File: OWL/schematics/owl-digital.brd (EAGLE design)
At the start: 59.6 x 55.9 mm, 69 parts, among them IC1 REG1117, IC3 IS61WV51216BLL-10TLI, Q1 12.288MHz, Q2 8MHz, U2 WM8731, U4 STM32F405ZGT6

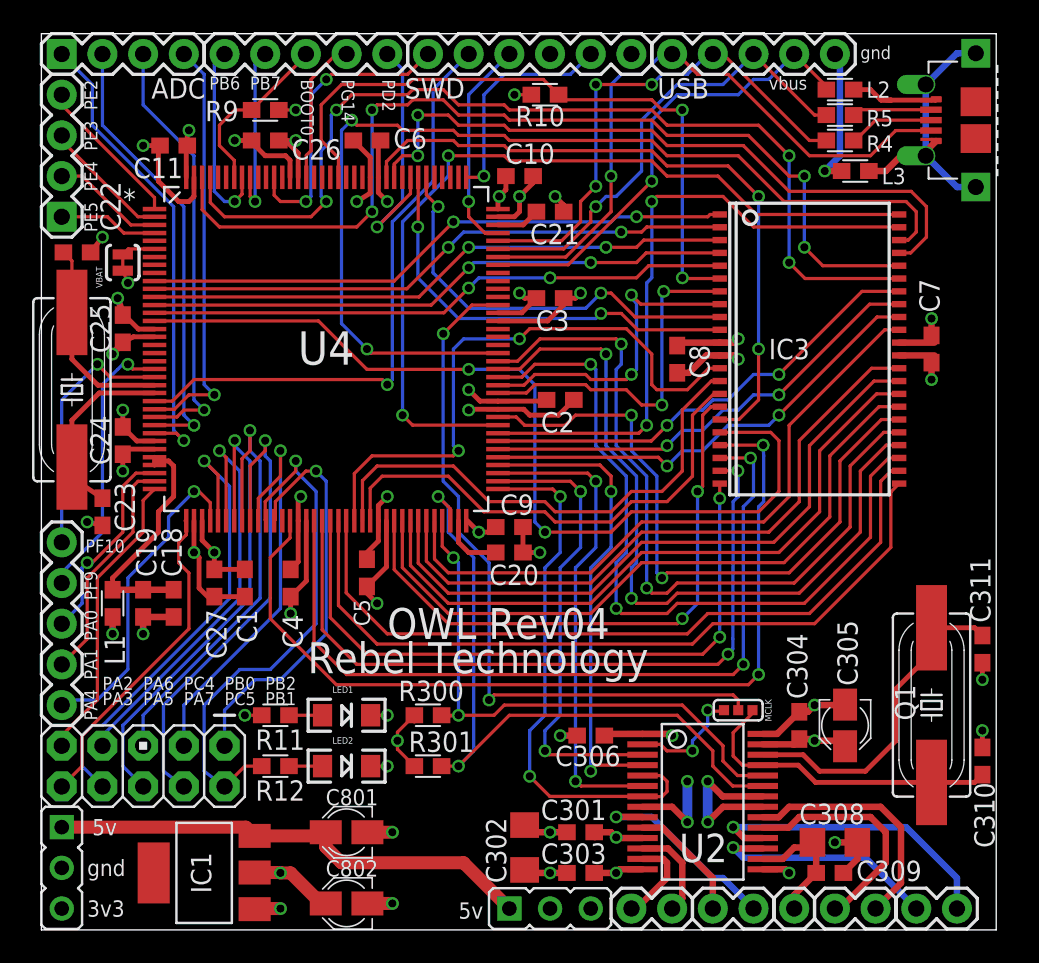
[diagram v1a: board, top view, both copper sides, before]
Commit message: changed for rev05: usb power routing via inductors, connected usb gnd.
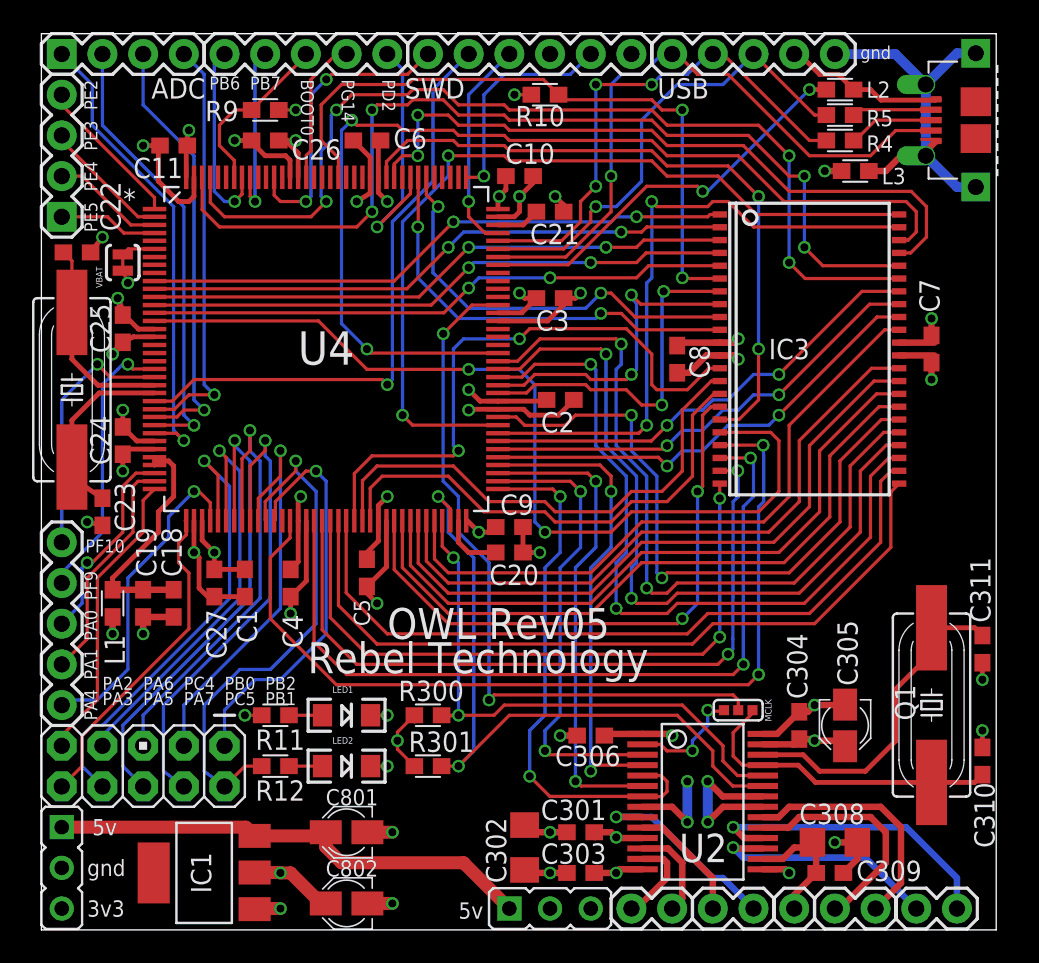
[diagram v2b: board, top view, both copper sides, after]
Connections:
- removed net N$1: L2.1, USB1.1, USB1.6
- removed net N$3: L3.1, USB1.5, USB1.7, USB1.G, USB1.G2, USB1.G3, USB1.G4
- new net VBUS: L2.2, U4.101
- net GND: now also L3.2
- net USB_GND: now also L3.1, USB1.5, USB1.7, USB1.G, USB1.G2, USB1.G3, USB1.G4; no longer L3.2
- net USB_VBUS: now also L2.1, USB1.1, USB1.6; no longer L2.2, U4.101
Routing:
- net VBUS: track 0.00 -> 25.3 mm, vias 0 -> 2
- net USB_VBUS: track 29.2 -> 11.0 mm, vias 1 -> 0
- net N$3: track 17.5 -> 0.00 mm
- net USB_GND: track 8.88 -> 23.9 mm, vias 1 -> 0
- net N$1: track 6.67 -> 0.00 mm
- net GND: track 111.6 -> 113.1 mm, vias 34 -> 35
- net +3V3: track 93.8 -> 94.8 mm
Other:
- board text added: "OWL Rev05"
- board text removed: "OWL Rev04"
- board text removed: "vbus"

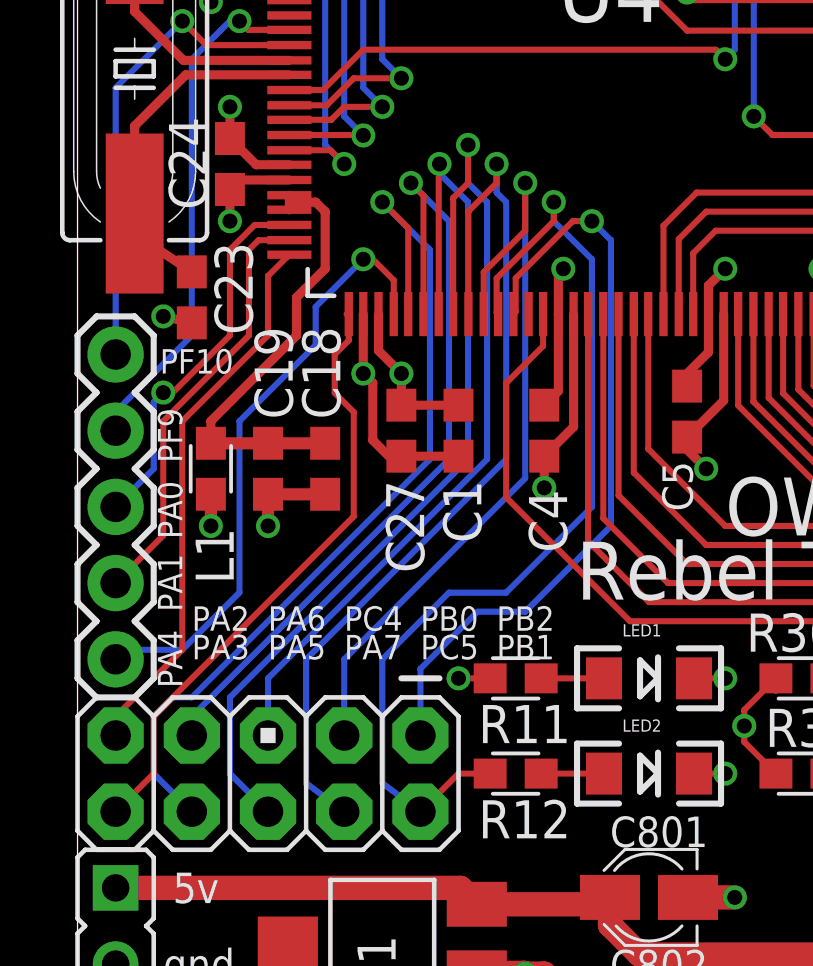
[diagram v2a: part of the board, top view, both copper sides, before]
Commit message: added pull-down resistor R13 from BOOT1/PD2 to gnd and tidied up schematic
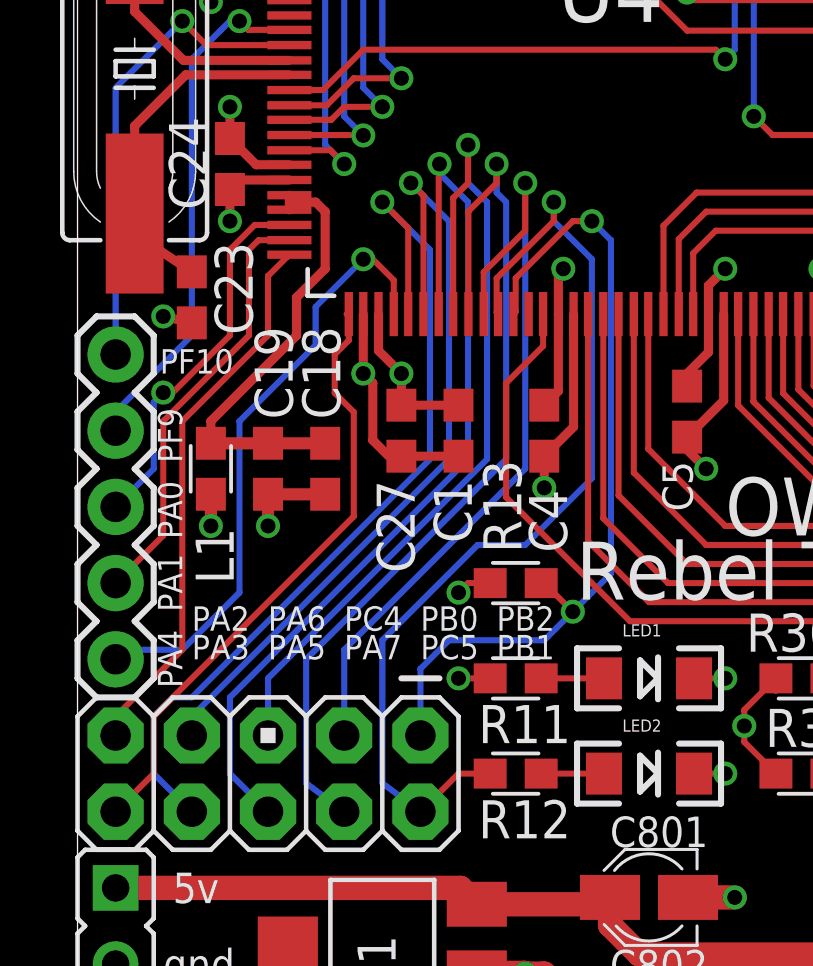
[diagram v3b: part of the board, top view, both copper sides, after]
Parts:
- added R13: 10K, Rebel:0603
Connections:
- removed net N$123: U4.19
- removed net N$124: U4.18
- net GND: now also R13.1
- net PB2: now also R13.2
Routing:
- net PB2: track 25.5 -> 27.9 mm, vias 1 -> 2
- net GND: track 113.1 -> 114.3 mm, vias 35 -> 36
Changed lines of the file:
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@@
 </element>
 <element name="C1" library="resistor" package="C0603" value="1u" x="12.7" y="22.225" smashed="yes" rot="R270">
-<attribute name="NAME" x="12.192" y="20.574" size="1.27" layer="25" rot="R270"/>
+<attribute name="NAME" x="11.8745" y="20.574" size="1.27" layer="25" rot="R270"/>
 <attribute name="VALUE" x="10.668" y="23.114" size="1.27" layer="27" rot="R270"/>
 </element>
@@
 </element>
 <element name="C27" library="resistor" package="C0603" value="100n" x="10.795" y="22.225" smashed="yes" rot="R270">
-<attribute name="NAME" x="10.287" y="20.574" size="1.27" layer="25" rot="R270"/>
+<attribute name="NAME" x="9.9695" y="20.574" size="1.27" layer="25" rot="R270"/>
 <attribute name="VALUE" x="8.763" y="23.114" size="1.27" layer="27" rot="R270"/>
 </element>
@@
 <attribute name="NAME" x="45.16954375" y="13.58138125" size="0.4064" layer="25" rot="R90" align="top-left"/>
 <attribute name="VALUE" x="44.7675" y="15.5575" size="0.4064" layer="27" rot="R180"/>
+</element>
+<element name="R13" library="Rebel" package="0603" value="10K" x="14.605" y="17.145" smashed="yes">
+<attribute name="NAME" x="14.7955" y="18.161" size="1.27" layer="25" rot="R90"/>
 </element>
 </elements>
@@
 <wire x1="50.165" y1="14.635" x2="49.7475" y2="14.635" width="0.4064" layer="1"/>
 <wire x1="49.7475" y1="14.635" x2="49.7175" y2="14.605" width="0.4064" layer="1"/>
+<contactref element="R13" pad="1"/>
+<wire x1="13.755" y1="17.145" x2="13.0175" y2="17.145" width="0.2032" layer="1"/>
+<wire x1="13.0175" y1="17.145" x2="12.7" y2="16.8275" width="0.2032" layer="1"/>
+<via x="12.7" y="16.8275" extent="1-16" drill="0.5"/>
 </signal>
 <signal name="+5V">
@@
 <contactref element="U4" pad="46"/>
 <via x="14.9225" y="30.48" extent="1-16" drill="0.5"/>
-<wire x1="14.9225" y1="30.48" x2="14.9225" y2="20.6375" width="0.2032" layer="16"/>
-<wire x1="14.9225" y1="20.6375" x2="8.89" y2="14.605" width="0.2032" layer="16"/>
-<wire x1="8.89" y1="14.605" x2="8.89" y2="12.065" width="0.2032" layer="16"/>
+<wire x1="14.9225" y1="30.48" x2="14.9225" y2="20.955" width="0.2032" layer="16"/>
+<wire x1="14.9225" y1="20.955" x2="8.89" y2="14.9225" width="0.2032" layer="16"/>
+<wire x1="8.89" y1="14.9225" x2="8.89" y2="12.065" width="0.2032" layer="16"/>
 <wire x1="13.5382" y1="26.1112" x2="13.5382" y2="27.5082" width="0.2032" layer="1"/>
 <wire x1="13.5382" y1="27.5082" x2="14.9225" y2="28.8925" width="0.2032" layer="1"/>
@@
 <via x="15.875" y="29.845" extent="1-16" drill="0.5"/>
 <wire x1="15.875" y1="29.845" x2="15.875" y2="29.21" width="0.2032" layer="16"/>
-<wire x1="17.145" y1="27.94" x2="17.145" y2="19.685" width="0.2032" layer="16"/>
-<wire x1="17.145" y1="19.685" x2="14.2875" y2="16.8275" width="0.2032" layer="16"/>
-<wire x1="14.2875" y1="16.8275" x2="12.3825" y2="16.8275" width="0.2032" layer="16"/>
-<wire x1="12.3825" y1="16.8275" x2="10.16" y2="14.605" width="0.2032" layer="16"/>
-<wire x1="10.16" y1="14.605" x2="10.16" y2="10.4775" width="0.2032" layer="16"/>
+<wire x1="17.145" y1="27.94" x2="17.145" y2="20.6375" width="0.2032" layer="16"/>
+<wire x1="17.145" y1="20.6375" x2="14.9225" y2="18.415" width="0.2032" layer="16"/>
+<wire x1="14.9225" y1="18.415" x2="13.335" y2="18.415" width="0.2032" layer="16"/>
+<wire x1="13.335" y1="18.415" x2="10.16" y2="15.24" width="0.2032" layer="16"/>
+<wire x1="10.16" y1="15.24" x2="10.16" y2="10.4775" width="0.2032" layer="16"/>
 <wire x1="10.16" y1="10.4775" x2="11.43" y2="9.525" width="0.2032" layer="16"/>
 <wire x1="13.97" y1="26.162" x2="13.97" y2="27.305" width="0.2032" layer="1"/>
@@
 <wire x1="14.5288" y1="26.1112" x2="14.605" y2="26.1874" width="0.2032" layer="1"/>
 <via x="17.145" y="29.21" extent="1-16" drill="0.5"/>
-<wire x1="17.78" y1="28.575" x2="17.78" y2="19.05" width="0.2032" layer="16"/>
-<wire x1="17.78" y1="19.05" x2="14.9225" y2="16.1925" width="0.2032" layer="16"/>
-<wire x1="14.9225" y1="16.1925" x2="13.335" y2="16.1925" width="0.2032" layer="16"/>
-<wire x1="13.335" y1="16.1925" x2="11.43" y2="14.2875" width="0.2032" layer="16"/>
+<wire x1="17.78" y1="28.575" x2="17.78" y2="17.4625" width="0.2032" layer="16"/>
 <wire x1="11.43" y1="14.2875" x2="11.43" y2="12.065" width="0.2032" layer="16"/>
 <wire x1="14.605" y1="26.1874" x2="14.605" y2="27.305" width="0.2032" layer="1"/>
@@
 <wire x1="16.51" y1="29.21" x2="17.145" y2="29.21" width="0.2032" layer="1"/>
 <wire x1="17.78" y1="28.575" x2="17.145" y2="29.21" width="0.2032" layer="16"/>
+<contactref element="R13" pad="2"/>
+<wire x1="15.455" y1="17.145" x2="15.5575" y2="17.145" width="0.2032" layer="1"/>
+<wire x1="15.5575" y1="17.145" x2="16.51" y2="16.1925" width="0.2032" layer="1"/>
+<via x="16.51" y="16.1925" extent="1-16" drill="0.5"/>
+<wire x1="11.43" y1="14.2875" x2="12.3825" y2="15.24" width="0.2032" layer="16"/>
+<wire x1="12.3825" y1="15.24" x2="15.5575" y2="15.24" width="0.2032" layer="16"/>
+<wire x1="15.5575" y1="15.24" x2="16.51" y2="16.1925" width="0.2032" layer="16"/>
+<wire x1="17.78" y1="17.4625" x2="16.51" y2="16.1925" width="0.2032" layer="16"/>
 </signal>
 <signal name="PB4">
@@
 </signal>
 <signal name="PA0">
-<contactref element="U4" pad="34"/>
-<wire x1="7.0612" y1="29.083" x2="5.9055" y2="29.083" width="0.2032" layer="1"/>
 <wire x1="5.9055" y1="29.083" x2="5.08" y2="28.2575" width="0.2032" layer="1"/>
 <wire x1="5.08" y1="28.2575" x2="5.08" y2="25.4" width="0.2032" layer="1"/>
@@
 <wire x1="2.54" y1="23.1775" x2="2.54" y2="20.955" width="0.2032" layer="16"/>
 <wire x1="2.54" y1="20.955" x2="1.27" y2="19.685" width="0.2032" layer="16"/>
+<contactref element="U4" pad="34"/>
+<wire x1="7.0612" y1="29.083" x2="5.9055" y2="29.083" width="0.2032" layer="1"/>
 </signal>
 <signal name="PA1">
@@
 <wire x1="6.0325" y1="28.575" x2="5.715" y2="28.2575" width="0.2032" layer="1"/>
 <wire x1="5.715" y1="28.2575" x2="5.715" y2="25.4" width="0.2032" layer="1"/>
-<wire x1="2.8575" y1="20.0025" x2="2.8575" y2="22.5425" width="0.2032" layer="1"/>
+<wire x1="2.8575" y1="18.7325" x2="2.8575" y2="22.5425" width="0.2032" layer="1"/>
 <wire x1="2.8575" y1="22.5425" x2="5.715" y2="25.4" width="0.2032" layer="1"/>
-<wire x1="2.8575" y1="20.0025" x2="2.8575" y2="18.7325" width="0.2032" layer="1"/>
-<wire x1="2.8575" y1="18.7325" x2="1.27" y2="17.145" width="0.2032" layer="1"/>
 <contactref element="JP3" pad="2"/>
+<wire x1="1.27" y1="17.145" x2="2.8575" y2="18.7325" width="0.2032" layer="1"/>
 </signal>
 <signal name="PA3">
@@
 <wire x1="4.7625" y1="35.56" x2="5.08" y2="35.8775" width="0.2032" layer="16"/>
 <wire x1="5.08" y1="35.8775" x2="5.3975" y2="35.8775" width="0.2032" layer="16"/>
-</signal>
-<signal name="N$123">
-<contactref element="U4" pad="19"/>
-</signal>
-<signal name="N$124">
-<contactref element="U4" pad="18"/>
 </signal>
 <signal name="PF0">
@@
 <signal name="USB_GND">
 <contactref element="USB" pad="5"/>
-<contactref element="USB1" pad="5" route="any" routetag="GND"/>
-<contactref element="USB1" pad="7" route="any" routetag="GND"/>
+<contactref element="USB1" pad="5" route="any" routetag="USB.GND"/>
+<contactref element="USB1" pad="7" route="any" routetag="USB.GND"/>
 <contactref element="L3" pad="1"/>
 <contactref element="USB1" pad="G2"/>

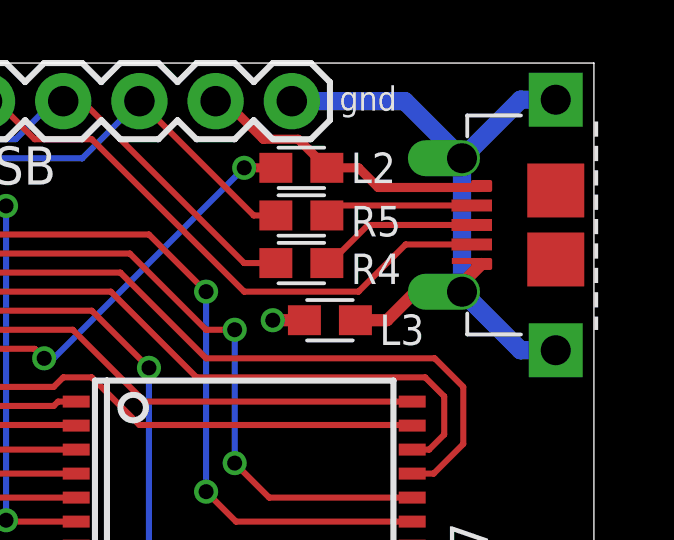
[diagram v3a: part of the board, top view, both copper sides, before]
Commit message: changed usb connector footprint: square pads, smaller drill, cream on th pads
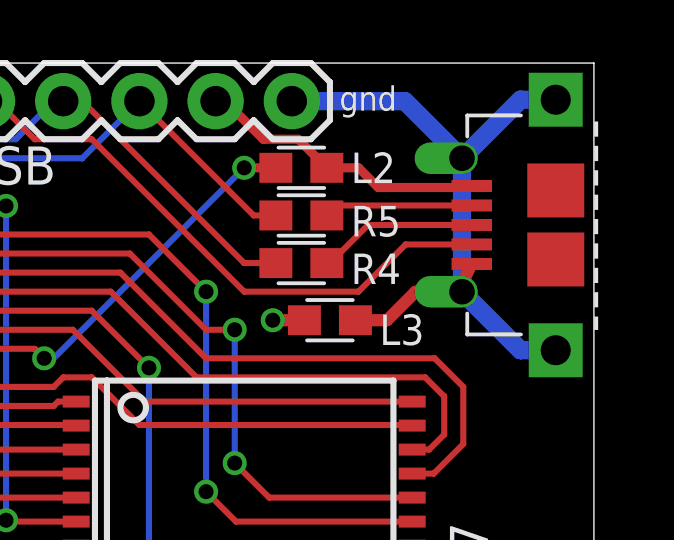
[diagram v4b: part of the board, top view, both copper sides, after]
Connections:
- net USB_GND: no longer USB1.7
- net USB_VBUS: no longer USB1.6
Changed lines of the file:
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@@
 <signal name="USB_GND">
 <contactref element="USB" pad="5"/>
-<contactref element="USB1" pad="5" route="any" routetag="USB.GND"/>
-<contactref element="USB1" pad="7" route="any" routetag="USB.GND"/>
+<contactref element="USB1" pad="5"/>
 <contactref element="L3" pad="1"/>
 <contactref element="USB1" pad="G2"/>
@@
 <wire x1="52.705" y1="47.9425" x2="51.65" y2="47.9425" width="0.4064" layer="1"/>
 <wire x1="55.2025" y1="48.8925" x2="55.2025" y2="49.1625" width="0.4064" layer="1"/>
-<wire x1="55.2025" y1="49.1625" x2="55.8575" y2="49.8175" width="0.4064" layer="1"/>
+<wire x1="55.2025" y1="49.1625" x2="55.5275" y2="49.8175" width="0.4064" layer="1"/>
 <wire x1="49.53" y1="55.245" x2="53.3" y2="55.245" width="0.6096" layer="16"/>
 <wire x1="53.3" y1="55.245" x2="55.2025" y2="53.3425" width="0.6096" layer="16"/>
@@
 <contactref element="USB" pad="4"/>
 <contactref element="USB1" pad="1"/>
-<contactref element="USB1" pad="6"/>
 <contactref element="L2" pad="1"/>
 <wire x1="51.7525" y1="53.0225" x2="50.6975" y2="53.0225" width="0.3048" layer="1"/>
 <wire x1="52.407559375" y1="52.367440625" x2="55.807440625" y2="52.367440625" width="0.3048" layer="1"/>
-<wire x1="55.807440625" y1="52.367440625" x2="55.8575" y2="52.4175" width="0.3048" layer="1"/>
+<wire x1="55.807440625" y1="52.367440625" x2="55.5275" y2="52.4175" width="0.3048" layer="1"/>
 <wire x1="55.807440625" y1="52.367440625" x2="55.287440625" y2="52.367440625" width="0.2032" layer="1"/>
 <wire x1="55.287440625" y1="52.367440625" x2="55.2375" y2="52.3175" width="0.2032" layer="1"/>

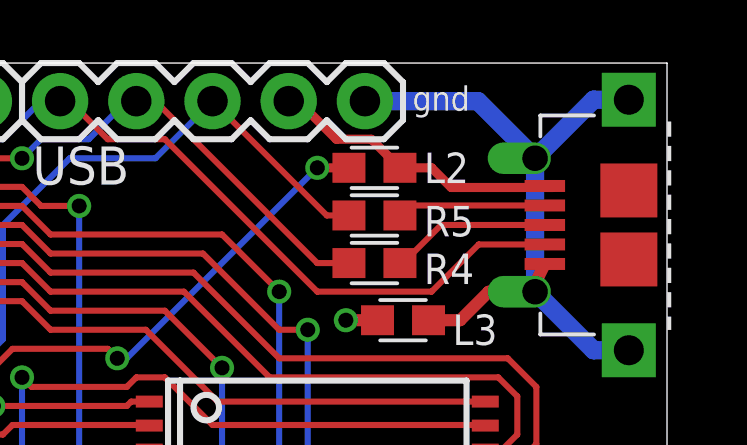
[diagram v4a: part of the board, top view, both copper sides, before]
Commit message: set values for BOM
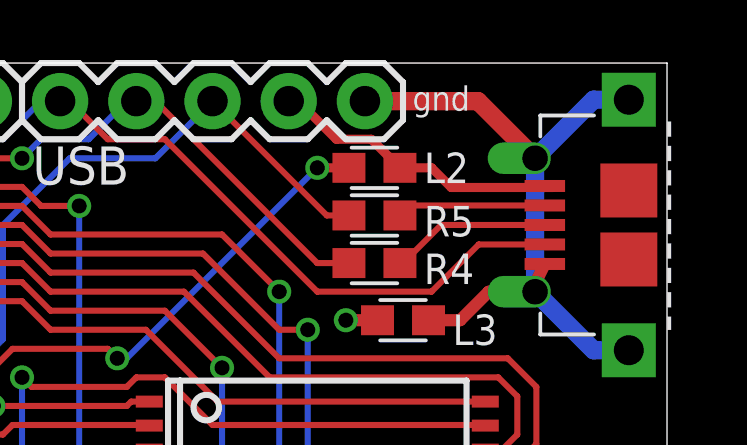
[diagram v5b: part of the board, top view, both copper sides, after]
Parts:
- IC1: value REG1117 -> TLV1117-33CDCY
- LED1, LED2: value (none) -> KP-3216SGC
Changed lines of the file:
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@@
 <attribute name="VALUE" x="50.7365" y="53.467" size="1.27" layer="27" rot="R180"/>
 </element>
-<element name="LED1" library="SparkFun" package="LED-1206" value="" x="19.05" y="13.97"/>
-<element name="LED2" library="SparkFun" package="LED-1206" value="" x="19.05" y="10.795"/>
+<element name="LED1" library="SparkFun" package="LED-1206" value="KP-3216SGC" x="19.05" y="13.97"/>
+<element name="LED2" library="SparkFun" package="LED-1206" value="KP-3216SGC" x="19.05" y="10.795"/>
 <element name="R11" library="Rebel" package="0603" value="1k" x="14.605" y="13.97" smashed="yes">
 <attribute name="NAME" x="16.4465" y="13.081" size="1.27" layer="25" rot="R180"/>
@@
 <attribute name="VALUE" x="8.763" y="23.114" size="1.27" layer="27" rot="R270"/>
 </element>
-<element name="IC1" library="burr-brown" package="SOT223" value="REG1117" x="10.16" y="4.1275" smashed="yes" rot="R90">
+<element name="IC1" library="burr-brown" package="SOT223" value="TLV1117-33CDCY" x="10.16" y="4.1275" smashed="yes" rot="R90">
 <attribute name="OC_NEWARK" value="14P6981" x="-2.54" y="-4.1275" size="1.778" layer="27" rot="R90" display="off"/>
 <attribute name="MPN" value="REG1117" x="-2.54" y="-4.1275" size="1.778" layer="27" rot="R90" display="off"/>
@@
 <wire x1="55.2025" y1="48.8925" x2="55.2025" y2="49.1625" width="0.4064" layer="1"/>
 <wire x1="55.2025" y1="49.1625" x2="55.5275" y2="49.8175" width="0.4064" layer="1"/>
-<wire x1="49.53" y1="55.245" x2="53.3" y2="55.245" width="0.6096" layer="16"/>
-<wire x1="53.3" y1="55.245" x2="55.2025" y2="53.3425" width="0.6096" layer="16"/>
+<wire x1="49.53" y1="55.245" x2="53.3" y2="55.245" width="0.6096" layer="1"/>
+<wire x1="53.3" y1="55.245" x2="55.2025" y2="53.3425" width="0.6096" layer="1"/>
 <wire x1="58.3275" y1="46.9425" x2="57.1525" y2="46.9425" width="0.6096" layer="16"/>
 <wire x1="57.1525" y1="46.9425" x2="55.2025" y2="48.8925" width="0.6096" layer="16"/>
